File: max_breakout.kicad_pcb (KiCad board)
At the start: 4 copper layers, 51.1 x 25.7 mm, 48 parts, among them J1 Left, J2 Right, J3 AVR-JTAG-10, J4 USB_B_Micro, Q1 IRLML6402, SW1 Reset, SW2 User, SW3 User DIP Switch, SW4 ENA Switch, U1 LP2985-5.0, U2 EPM7032STC44, U3 DS1813R-5+T&R, U4 MAX40203AUK+T, U5 LP2985-3.3, U6 74HCT244, X1 CTX-636 50mhz

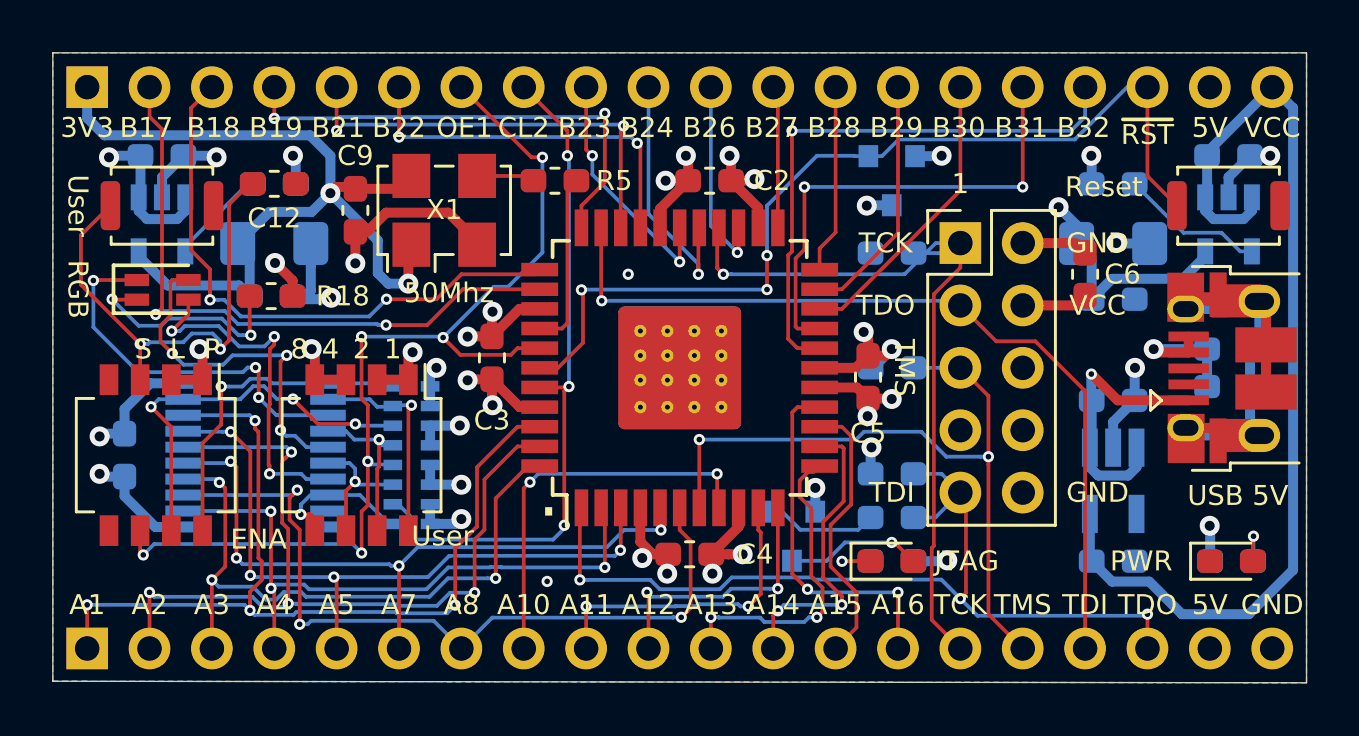
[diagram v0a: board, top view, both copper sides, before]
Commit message: reorganized part layout, replace mosfet with inverter
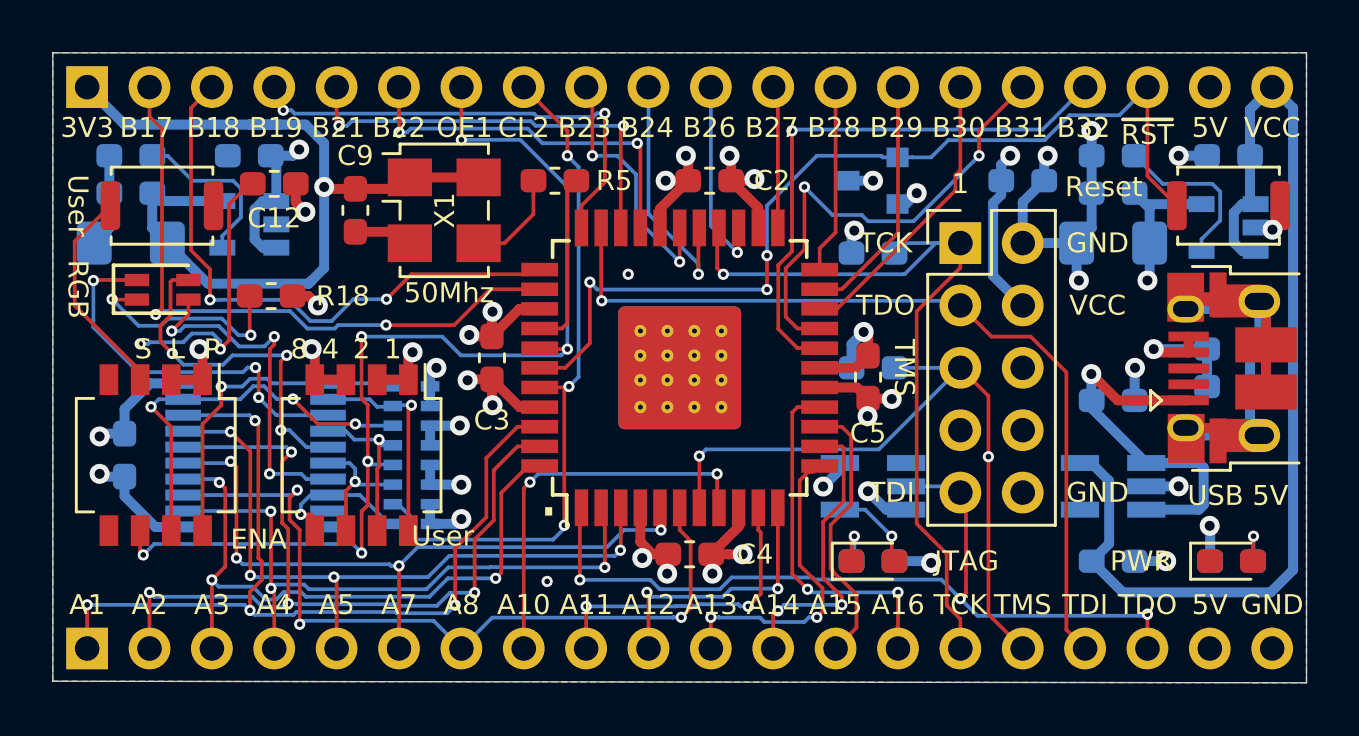
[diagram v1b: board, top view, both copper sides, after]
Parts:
- removed Q1: IRLML6402, Package_TO_SOT_SMD:SOT-23
- removed R4: 10K, Resistor_SMD:R_0603_1608Metric_Pad1.05x0.95mm_HandSolder
- removed R7: 100R, Resistor_SMD:R_0603_1608Metric_Pad1.05x0.95mm_HandSolder
- added U7: 74LVC1G04, Package_TO_SOT_SMD:SOT-23-5_HandSoldering, B.Cu at (157.7, 109.0)
- C6: moved to B.Cu
- moved C16 7.09 mm to (127.5, 97.0), turned to 180 degrees
- moved C14 5.95 mm to (127.5, 95.5), turned to 180 degrees
- moved C19 5.84 mm to (127.5, 99.1), turned to 180 degrees
- moved C6 4.58 mm to (163.8, 96.5), turned to 0 degrees
- moved C17 4.32 mm to (167.5, 97.0), turned to 180 degrees
- moved C1 3.56 mm to (132.3, 95.5), turned to 180 degrees
- moved U5 3.56 mm to (132.3, 98.3), turned to 180 degrees
- moved C15 1.14 mm to (167.5, 95.5)
- moved R1 0.78 mm to (157.7, 99.5)
- moved R2 0.78 mm to (157.7, 104.1)
- moved R8 0.78 mm to (157.7, 112.0)
- moved D2 0.76 mm to (157.7, 112.0)
- moved U3 0.76 mm to (157.7, 96.5), turned to 180 degrees
- moved U4 0.22 mm to (167.5, 109.0), turned to 180 degrees
- moved U1 0.13 mm to (172.2, 98.4), turned to 180 degrees
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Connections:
- C1 pad 1: +5V -> VCC
- C10 pad 1: VCC -> /V_in
- C11 pad 1: VCC -> /V_in
- C17 pad 1: +5V -> VCC
- C18 pad 1: +5V -> VCC
- C2 pad 1: +5V -> VCC
- C3 pad 1: +5V -> VCC
- C4 pad 1: +5V -> VCC
- C5 pad 1: +5V -> VCC
- C6 pad 1: +5V -> VCC
- C7 pad 1: +5V -> VCC
- J1 pad 19: +5V -> VCC
- J2 pad 19: +5V -> VCC
- J2 pad 20: VCC -> /V_in
- J3 pad 4: +5V -> VCC
- R18 pad 1: +5V -> VCC
- R2 pad 1: +5V -> VCC
- R6 pad 1: +5V -> VCC
- RN1 pad 1: +5V -> VCC
- RN1 pad 2: +5V -> VCC
- RN1 pad 3: +5V -> VCC
- RN1 pad 4: +5V -> VCC
- RN1 pad 5: +5V -> VCC
- RN1 pad 6: +5V -> VCC
- RN1 pad 7: +5V -> VCC
- RN1 pad 8: +5V -> VCC
- U1 pad 1: VCC -> /V_in
- U1 pad 3: VCC -> /V_in
- U1 pad 5: +5V -> VCC
- U2 pad 17: +5V -> VCC
- U2 pad 29: +5V -> VCC
- U2 pad 41: +5V -> VCC
- U2 pad 9: +5V -> VCC
- U3 pad 2: +5V -> VCC
- U4 pad 5: VCC -> /V_in
- U5 pad 1: +5V -> VCC
- U5 pad 3: +5V -> VCC
- U6 pad 20: +5V -> VCC
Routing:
- net +5V: track 54.8 -> 0.00 mm, vias 20 -> 0
- net /V_in: track 0.00 -> 42.7 mm
- net VCC: track 40.3 -> 57.0 mm, vias 0 -> 19
- net Net-(Q1-Pad1): track 4.67 -> 0.00 mm
- net Net-(C8-Pad1): track 11.1 -> 15.3 mm
- net Net-(C14-Pad1): track 3.60 -> 6.89 mm
- net Net-(R5-Pad1): track 2.37 -> 5.42 mm
- net GND: track 65.5 -> 67.9 mm, vias 25 -> 28
- net /OE1: track 41.6 -> 43.9 mm
- net /TDI: track 37.1 -> 34.9 mm
- net Net-(D2-Pad2): track 5.56 -> 3.62 mm
- net /TCK: track 31.1 -> 32.9 mm
- net /~RST: track 37.4 -> 38.6 mm
- net Net-(C15-Pad1): track 5.91 -> 6.81 mm
- net /B23: track 10.1 -> 10.7 mm
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- added copper zone on In2.Cu, net VCC
- removed copper zone on In2.Cu, net +5V
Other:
- board text added: "MAX7000S Breakout Board v2.2 by Hyiger Designs"
- board text removed: "MAX7000S Breakout Board v2.1 by Hyiger Designs"

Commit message: track cleanup
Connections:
- net +3V3 renamed 3V3
- net /V_in renamed Vin
- net VCC renamed 5V

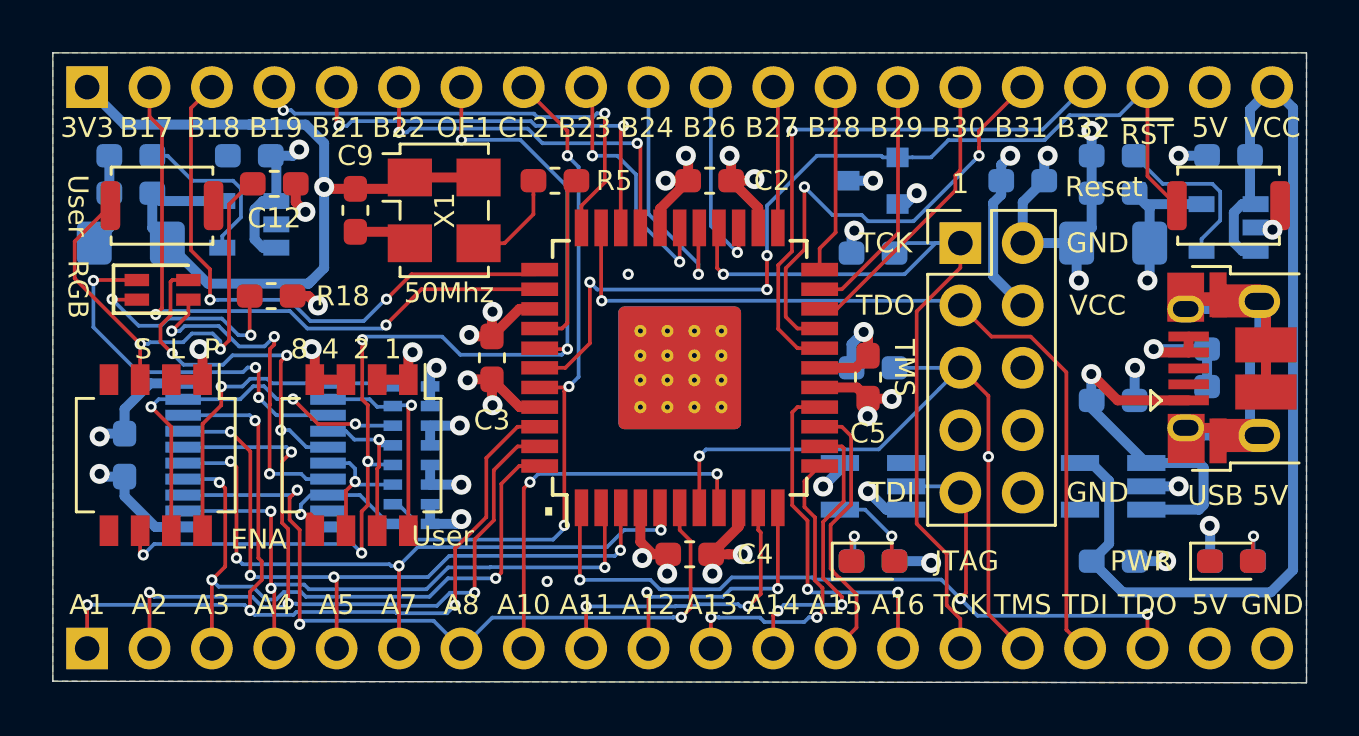
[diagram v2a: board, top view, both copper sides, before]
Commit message: removed switches
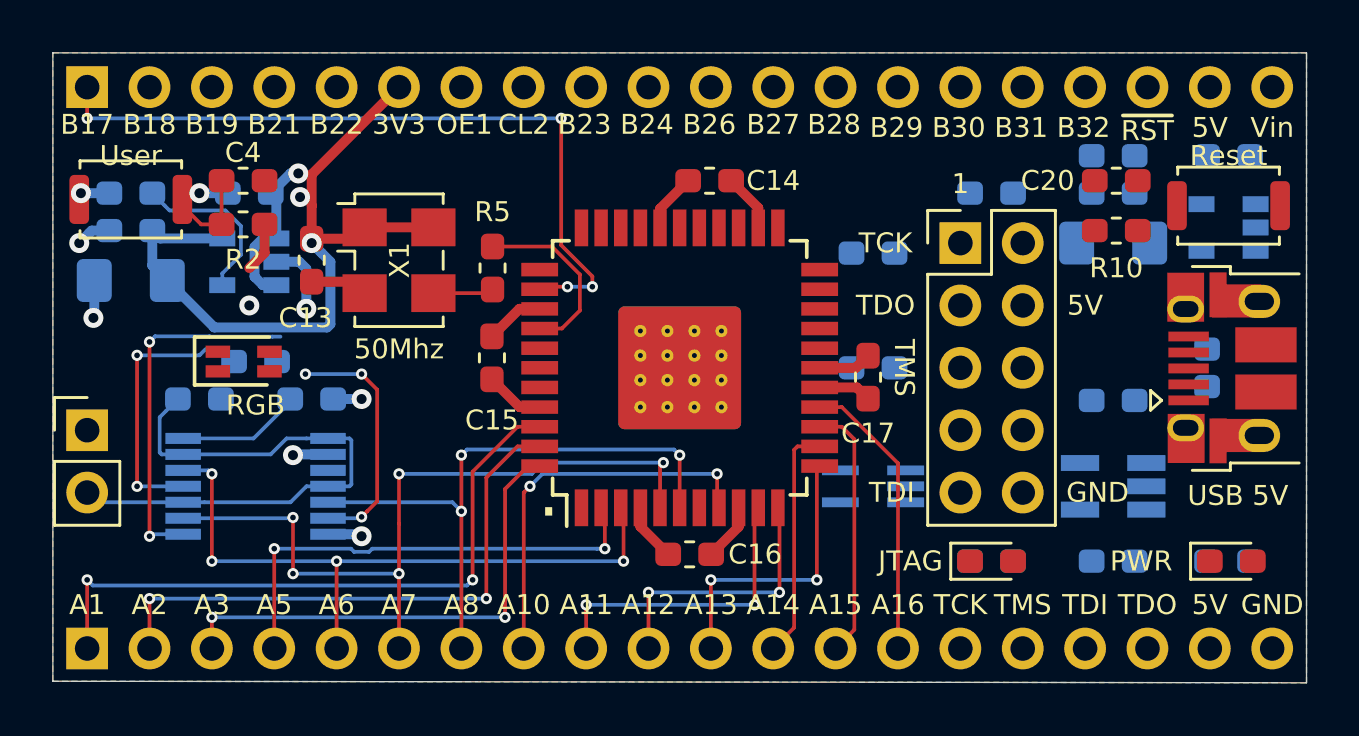
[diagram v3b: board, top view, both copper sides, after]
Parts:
- removed the C12 at (133.3, 96.6)
- removed the C9 at (136.7, 97.7)
- removed RN1: 10K, Resistor_SMD:R_Cat16-8
- removed the SW1 at (172.2, 97.5)
- removed SW3: User DIP Switch, Button_Switch_SMD:SW_DIP_SPSTx04_Slide_Omron_A6H-4101_W6.15mm_P1.27mm
- removed SW4: ENA Switch, Button_Switch_SMD:SW_DIP_SPSTx04_Slide_Omron_A6H-4101_W6.15mm_P1.27mm
- removed U3: DS1813R-5+T&R, Package_TO_SOT_SMD:SOT-23
- removed U6: 74HCT244, Package_SO:TSSOP-20_4.4x6.5mm_P0.65mm
- added C13: 100nF, Capacitor_SMD:C_0603_1608Metric_Pad1.05x0.95mm_HandSolder, F.Cu at (134.9, 99.8)
- added C20: 10nF, Capacitor_SMD:C_0603_1608Metric_Pad1.05x0.95mm_HandSolder, F.Cu at (167.6, 96.5)
- added C4: 10nF, Capacitor_SMD:C_0603_1608Metric_Pad1.05x0.95mm_HandSolder, F.Cu at (132.1, 96.5)
- added JP1: ena, Connector_PinHeader_2.54mm:PinHeader_1x02_P2.54mm_Vertical, F.Cu at (125.7, 106.7)
- added R10: 10K, Resistor_SMD:R_0603_1608Metric_Pad1.05x0.95mm_HandSolder, F.Cu at (167.6, 98.6)
- added R2: 10K, Resistor_SMD:R_0603_1608Metric_Pad1.05x0.95mm_HandSolder, F.Cu at (132.1, 98.3)
- added R9: 10K, Resistor_SMD:R_0603_1608Metric_Pad1.05x0.95mm_HandSolder, B.Cu at (130.3, 105.4)
- added SW2: Reset, Button_Switch_SMD:SW_Push_SPST_NO_Alps_SKRK, F.Cu at (172.2, 97.5)
- added U5: 74HCT125, Package_SO:TSSOP-14_4.4x5mm_P0.65mm, B.Cu at (132.6, 109.0)
- R4: renamed from R18; moved to B.Cu
- U8: renamed from U7; value 74LVC1G04 -> 74HCT1G04; footprint Package_TO_SOT_SMD:SOT-23-5_HandSoldering -> Package_TO_SOT_SMD:SOT-353_SC-70-5_Handsoldering
- moved C18 7.96 mm to (134.9, 105.4), turned to 0 degrees
- moved D3 4.83 mm to (162.6, 112.0)
- moved R8 4.83 mm to (162.6, 112.0)
- moved D2 4.41 mm to (132.1, 103.9)
- moved R5 4.37 mm to (142.2, 100.1), turned to 90 degrees
- moved X1 2.74 mm to (138.4, 99.8)
- moved R4 2.74 mm to (132.6, 103.9)
- moved C11 1.52 mm to (127.5, 100.6)
- moved C3 1.52 mm to (132.3, 97.0)
- moved C7 1.52 mm to (127.5, 97.0)
- moved C9 1.52 mm to (127.5, 98.6)
- moved U2 1.52 mm to (132.3, 99.8)
- moved C19 1.37 mm to (162.6, 97.0)
- moved SW1 1.30 mm to (127.5, 97.3), turned to 180 degrees
- moved R3 0.13 mm to (172.2, 112.0)
- renumbered C13 to C1, C18 to C10, C19 to C11, C10 to C12, C2 to C14, C3 to C15, C4 to C16, C5 to C17, C7 to C18, C6 to C19, C11 to C2, C1 to C3, C8 to C5, C15 to C6, C14 to C7, C17 to C8, C16 to C9, D3 to D2, D2 to D3, J4 to J1, J1 to J2, J2 to J4, R16 to R1, R6 to R3, R2 to R6, R1 to R7, SW2 to SW1, U5 to U2, U2 to U7
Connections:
- J4 pad 1: 3V3 -> /B17
- J4 pad 2: /B17 -> /B18
- J4 pad 3: /B18 -> /B19
- J4 pad 4: /B19 -> /B21
- J4 pad 5: /B21 -> /B22
- J4 pad 6: /B22 -> 3V3
- SW1 pad 1: Net-(C12-Pad1) -> /OE1
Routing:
- net GND: track 67.9 -> 23.9 mm, vias 28 -> 9
- net Vin: track 42.7 -> 0.00 mm
- net /OE1: track 43.8 -> 3.69 mm, vias 6 -> 0
- net /~RST: track 38.6 -> 0.00 mm, vias 3 -> 0
- net /TDI: track 34.9 -> 0.00 mm, vias 3 -> 0
- net /TDO: track 34.4 -> 0.00 mm, vias 1 -> 0
- net 5V: track 57.0 -> 23.1 mm, vias 19 -> 2
- net /TCK: track 32.9 -> 0.00 mm, vias 1 -> 0
- net /TMS: track 29.4 -> 0.00 mm, vias 2 -> 0
- net /CLK2: track 28.3 -> 0.00 mm, vias 3 -> 0
- net /B18: track 24.0 -> 0.00 mm, vias 2 -> 0
- net /ENA: track 0.00 -> 23.7 mm
- net /B32: track 23.0 -> 0.00 mm, vias 1 -> 0
- net Net-(C1-Pad1): track 20.0 -> 0.00 mm
- net Net-(C12-Pad1): track 19.9 -> 0.00 mm, vias 2 -> 0
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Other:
- board text added: "A6"
- board text added: "MAX7000S Breakout Board v3.0 by Hyiger Designs"
- board text added: "Vin"
- board text removed: "2"
- board text removed: "4"
- board text removed: "8"
- board text removed: "A4"
- board text removed: "ENA"
- board text removed: "L"
- board text removed: "MAX7000S Breakout Board v2.2 by Hyiger Designs"
- board text removed: "P"
- board text removed: "S"
- board text removed: "VCC"

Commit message: finished routing
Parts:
- moved C12 9.66 mm to (167.1, 102.4), turned to 180 degrees
- moved U4 3.83 mm to (167.1, 105.2)
- moved C5 2.51 mm to (167.1, 108.0), turned to 180 degrees
- moved D2 0.26 mm to (132.4, 103.9)
- moved C18 0.25 mm to (134.6, 105.4)
- moved R4 0.25 mm to (132.3, 103.9)
- moved R9 0.25 mm to (130.0, 105.4)
- moved U5 0.25 mm to (132.3, 109.0)
- moved D1 0.11 mm to (172.2, 112.0)
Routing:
- net /~RST: track 0.00 -> 40.8 mm, vias 0 -> 4
- net /TDI: track 0.00 -> 35.1 mm, vias 0 -> 3
- net /TDO: track 0.00 -> 34.6 mm, vias 0 -> 1
- net GND: track 23.9 -> 58.0 mm, vias 9 -> 32
- net /TCK: track 0.00 -> 30.1 mm, vias 0 -> 1
- net /TMS: track 0.00 -> 28.2 mm, vias 0 -> 1
- net /OE1: track 3.69 -> 31.9 mm, vias 0 -> 3
- net /B18: track 0.00 -> 27.6 mm, vias 0 -> 2
- net 5V: track 23.1 -> 50.7 mm, vias 2 -> 15
- net /B19: track 0.00 -> 20.9 mm, vias 0 -> 2
- net /B21: track 0.00 -> 20.0 mm, vias 0 -> 2
- net /B22: track 0.00 -> 18.1 mm, vias 0 -> 2
- net Vin: track 0.00 -> 18.0 mm
- net Net-(C1-Pad1): track 0.00 -> 17.6 mm
- net /B32: track 0.00 -> 16.1 mm
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
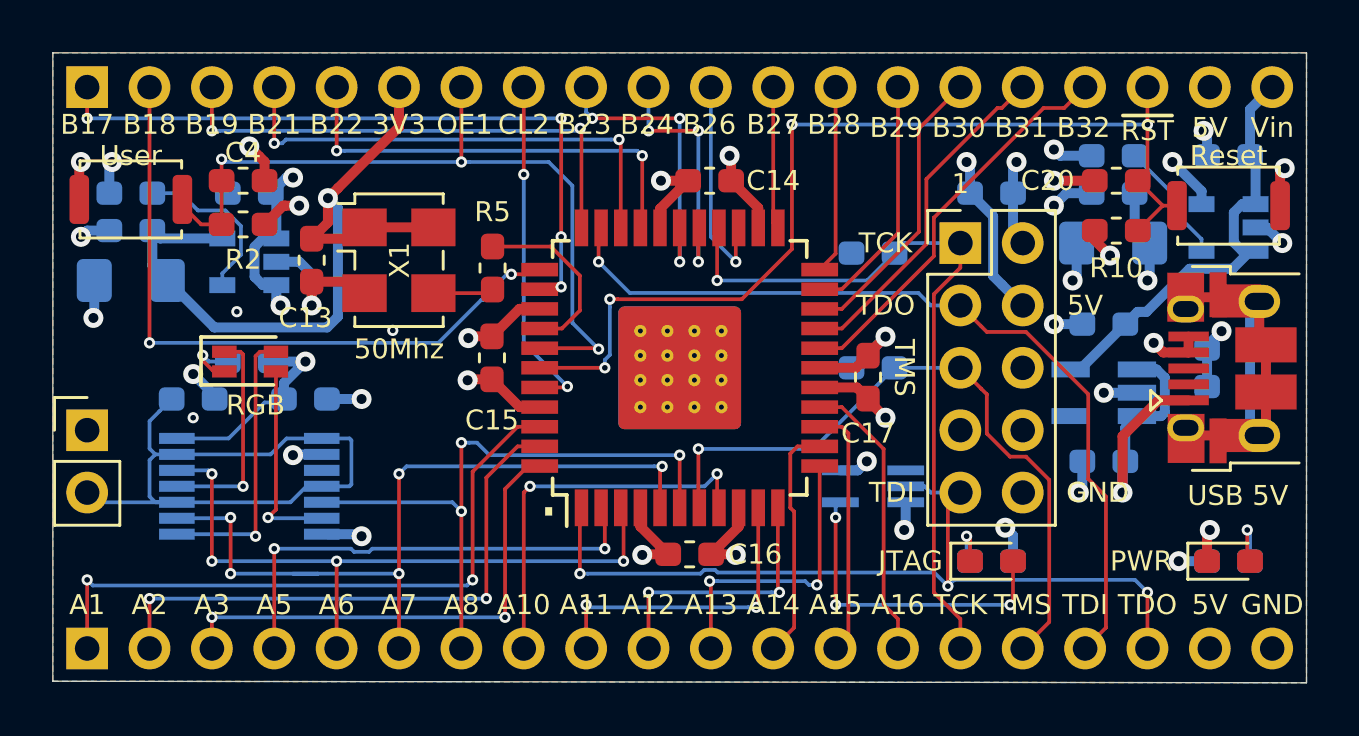
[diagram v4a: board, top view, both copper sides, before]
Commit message: fixed gnd breaks
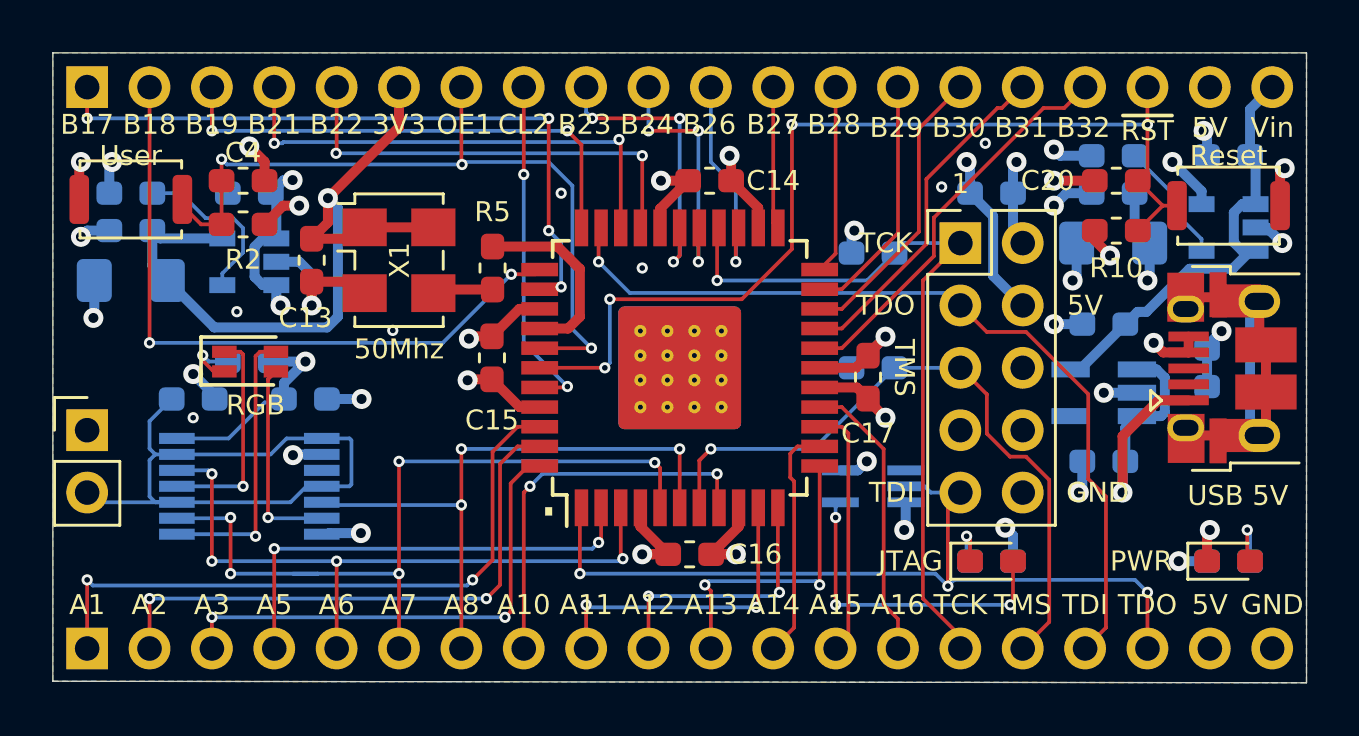
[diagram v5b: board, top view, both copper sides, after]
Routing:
- net GND: track 58.0 -> 58.9 mm, vias 32 -> 37
- net /A5: track 19.4 -> 18.8 mm
